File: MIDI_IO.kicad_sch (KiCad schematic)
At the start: 9 parts, among them J1 MIDI In, J7 MIDI Through, U1 6N137, U4 TL072

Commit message: add gerbers and bom
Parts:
- D1: LCSC (none) -> C2128; LCSC PN C2128 -> (none)
- J1, J7: JLCPCB_IGNORE (none) -> 1
- R1, R5, R6: LCSC (none) -> C22962
- R2: LCSC (none) -> C25804
- U1: LCSC (none) -> C15825; LCSC PN C15825 -> (none)
- U4: LCSC (none) -> C6961; LCSC PN C6961 -> (none)
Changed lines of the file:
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@@
 			)
 		)
-		(property "LCSC PN" ""
+		(property "LCSC" "C25804"
+			(at 120.65 43.18 0)
+			(effects
+				(font
+					(size 1.27 1.27)
+				)
+				(hide yes)
+			)
+		)
+		(property "JLCPCB_IGNORE" ""
 			(at 120.65 43.18 0)
 			(effects
@@
 			)
 		)
-		(property "LCSC PN" ""
+		(property "LCSC" "C22962"
+			(at 81.28 116.84 90)
+			(effects
+				(font
+					(size 1.27 1.27)
+				)
+				(hide yes)
+			)
+		)
+		(property "JLCPCB_IGNORE" ""
 			(at 81.28 116.84 90)
 			(effects
@@
 			)
 		)
-		(property "LCSC PN" ""
+		(property "JLCPCB_IGNORE" "1"
 			(at 106.68 119.38 0)
 			(effects
@@
 			)
 		)
-		(property "LCSC PN" "C2128"
+		(property "LCSC" "C2128"
+			(at 86.36 49.53 90)
+			(effects
+				(font
+					(size 1.27 1.27)
+				)
+				(hide yes)
+			)
+		)
+		(property "JLCPCB_IGNORE" ""
 			(at 86.36 49.53 90)
 			(effects
@@
 			)
 		)
-		(property "LCSC PN" "C6961"
+		(property "LCSC" "C6961"
+			(at 69.85 119.38 0)
+			(effects
+				(font
+					(size 1.27 1.27)
+				)
+				(hide yes)
+			)
+		)
+		(property "JLCPCB_IGNORE" ""
 			(at 69.85 119.38 0)
 			(effects
@@
 			)
 		)
-		(property "LCSC PN" ""
+		(property "JLCPCB_IGNORE" "1"
 			(at 60.96 48.26 0)
 			(effects
@@
 			)
 		)
-		(property "LCSC PN" "C15825"
+		(property "LCSC" "C15825"
+			(at 100.33 48.26 0)
+			(effects
+				(font
+					(size 1.27 1.27)
+				)
+				(hide yes)
+			)
+		)
+		(property "JLCPCB_IGNORE" ""
 			(at 100.33 48.26 0)
 			(effects
@@
 			)
 		)
-		(property "LCSC PN" ""
+		(property "LCSC" "C22962"
+			(at 76.2 45.72 90)
+			(effects
+				(font
+					(size 1.27 1.27)
+				)
+				(hide yes)
+			)
+		)
+		(property "JLCPCB_IGNORE" ""
 			(at 76.2 45.72 90)
 			(effects
@@
 			)
 		)
-		(property "LCSC PN" ""
+		(property "LCSC" "C22962"
 			(at 81.28 119.38 90)
 			(effects
+				(font
+					(size 1.27 1.27)
+				)
+				(hide yes)
+			)
+		)
+		(property "JLCPCB_IGNORE" ""
+			(at 81.28 119.38 90)
+			(effects

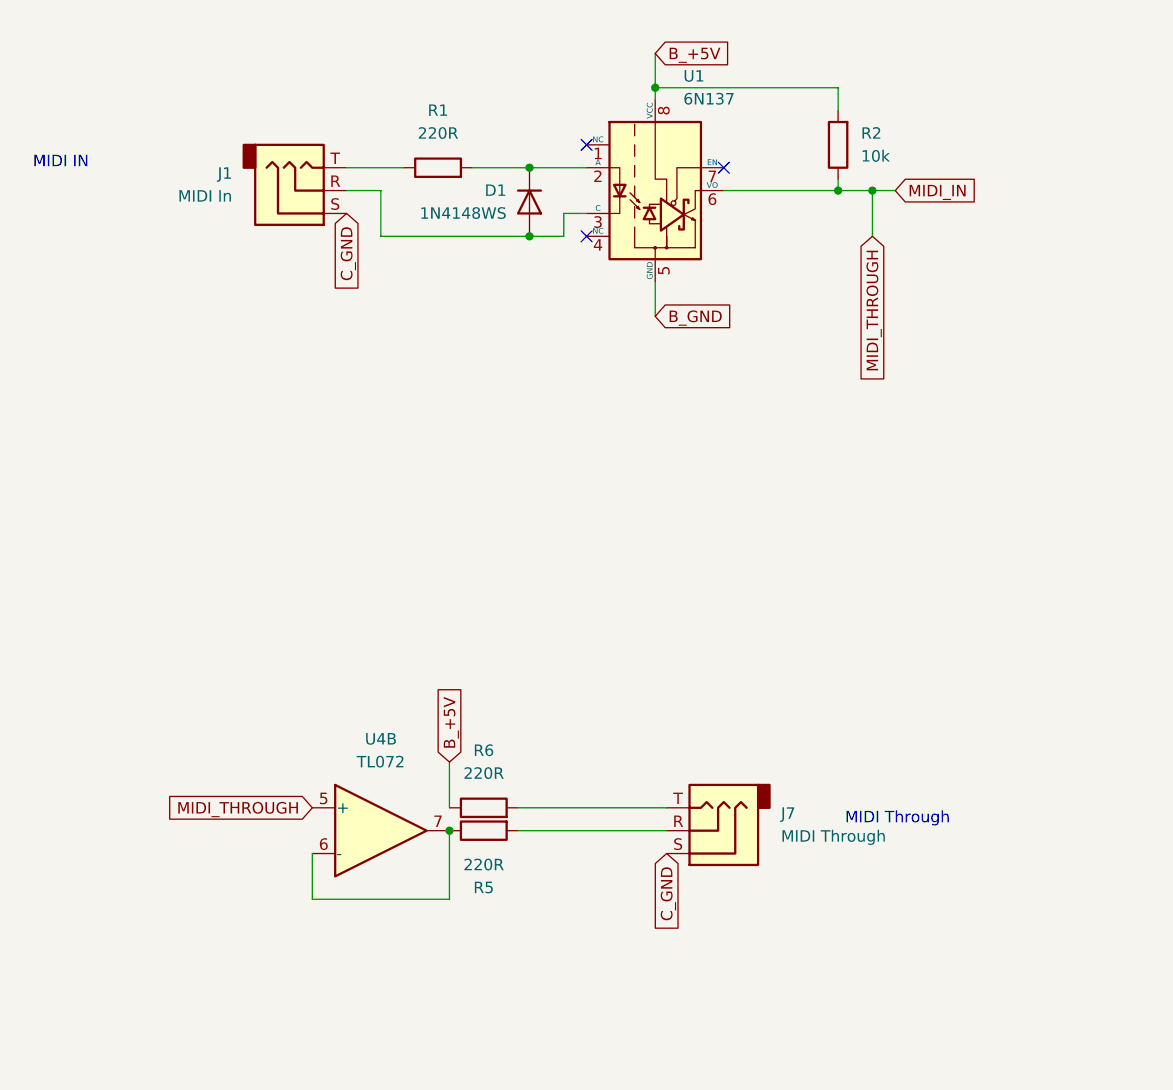
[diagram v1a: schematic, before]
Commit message: add rev 2 and rev 3, now with correct trs midi A
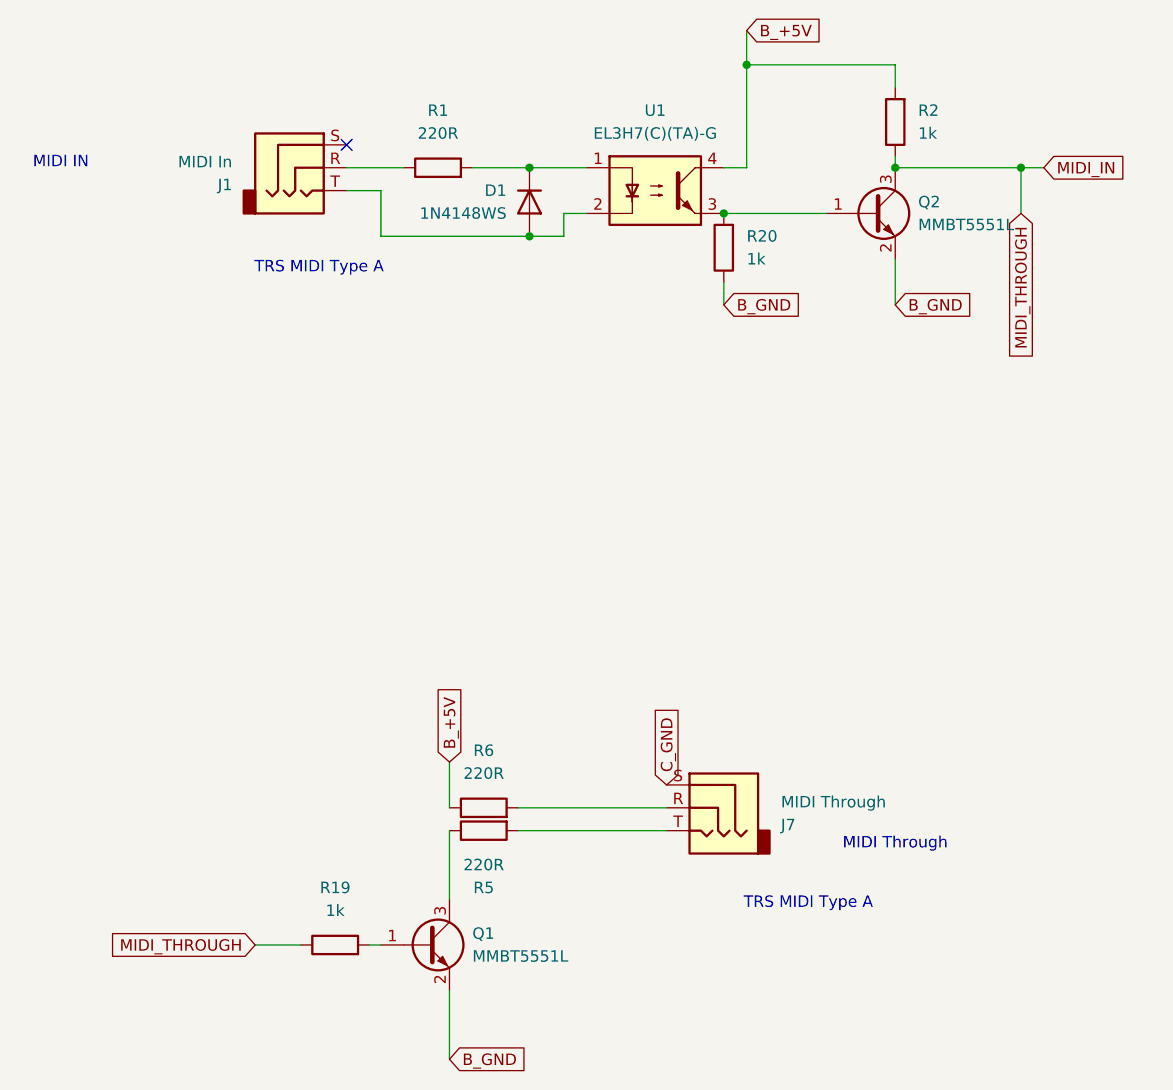
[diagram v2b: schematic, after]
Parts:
- removed U1: 6N137, Package_SO:SOP-8_6.605x9.655mm_P2.54mm, symbol Isolator:6N137
- removed U4: TL072, Package_SO:SOIC-8_3.9x4.9mm_P1.27mm, symbol Amplifier_Operational:TL072
- added Q1, Q2: MMBT5551L, Package_TO_SOT_SMD:SOT-23, symbol Transistor_BJT:MMBT5551L
- added R19, R20: 1k, Resistor_SMD:R_0603_1608Metric, symbol Device:R
- added U1: EL3H7(C)(TA)-G, Package_SO:SSOP-4_4.4x2.6mm_P1.27mm, symbol Isolator:Optocoupler_DC_PhotoNPN_AKEC
- R2: value 10k -> 1k; LCSC C25804 -> C21190
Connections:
- net B_+5V: now also U1.4
- net B_GND: now also Q1.2 (E), Q2.2 (E), R20.1
- net C_GND: no longer J1.S
- net MIDI_IN: now also Q2.3 (C), R19.1
- net at R6.2: now also J7.R; no longer J7.T
- net at R5.2: now also J7.T; no longer J7.R
- net at D1.1 (K), R1.2: now also U1.1
- net at D1.2 (A): now also J1.T, U1.2; no longer J1.R
- net at R5.1: now also Q1.3 (C)
- net at R1.1: now also J1.R; no longer J1.T
- new net: Q2.1 (B), R20.2, U1.3
- new net: Q1.1 (B), R19.2
- no-connect marks 3 -> 1
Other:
- note added: "TRS MIDI Type A"
- moved on the sheet: J1, J7, R2
